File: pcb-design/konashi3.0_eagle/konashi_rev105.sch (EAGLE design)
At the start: 33 parts, among them CN1 ZX62-B-5PA(11), CN2 S2B-PH-K-S, CN3 WML-C69, CN4 MA05-2-2, CN7 BK-913, IC1 LP2981-30DBVR, IC2 ZLDO1117G50DITR-ND

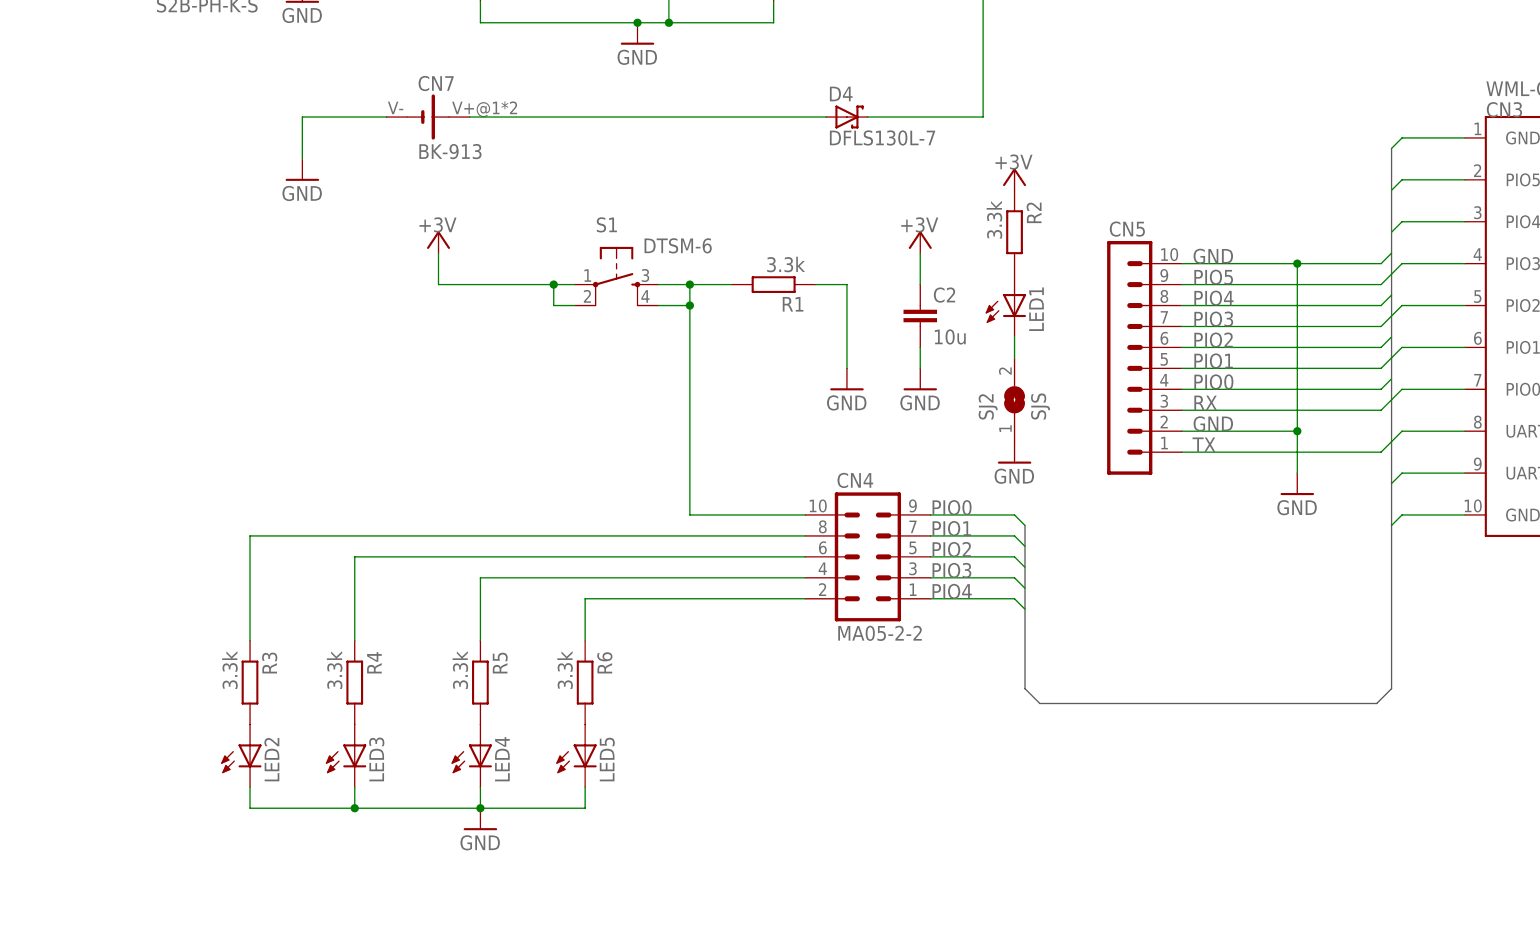
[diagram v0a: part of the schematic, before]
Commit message: 500kohm追加、ジャンパ用ピンヘッダ変更
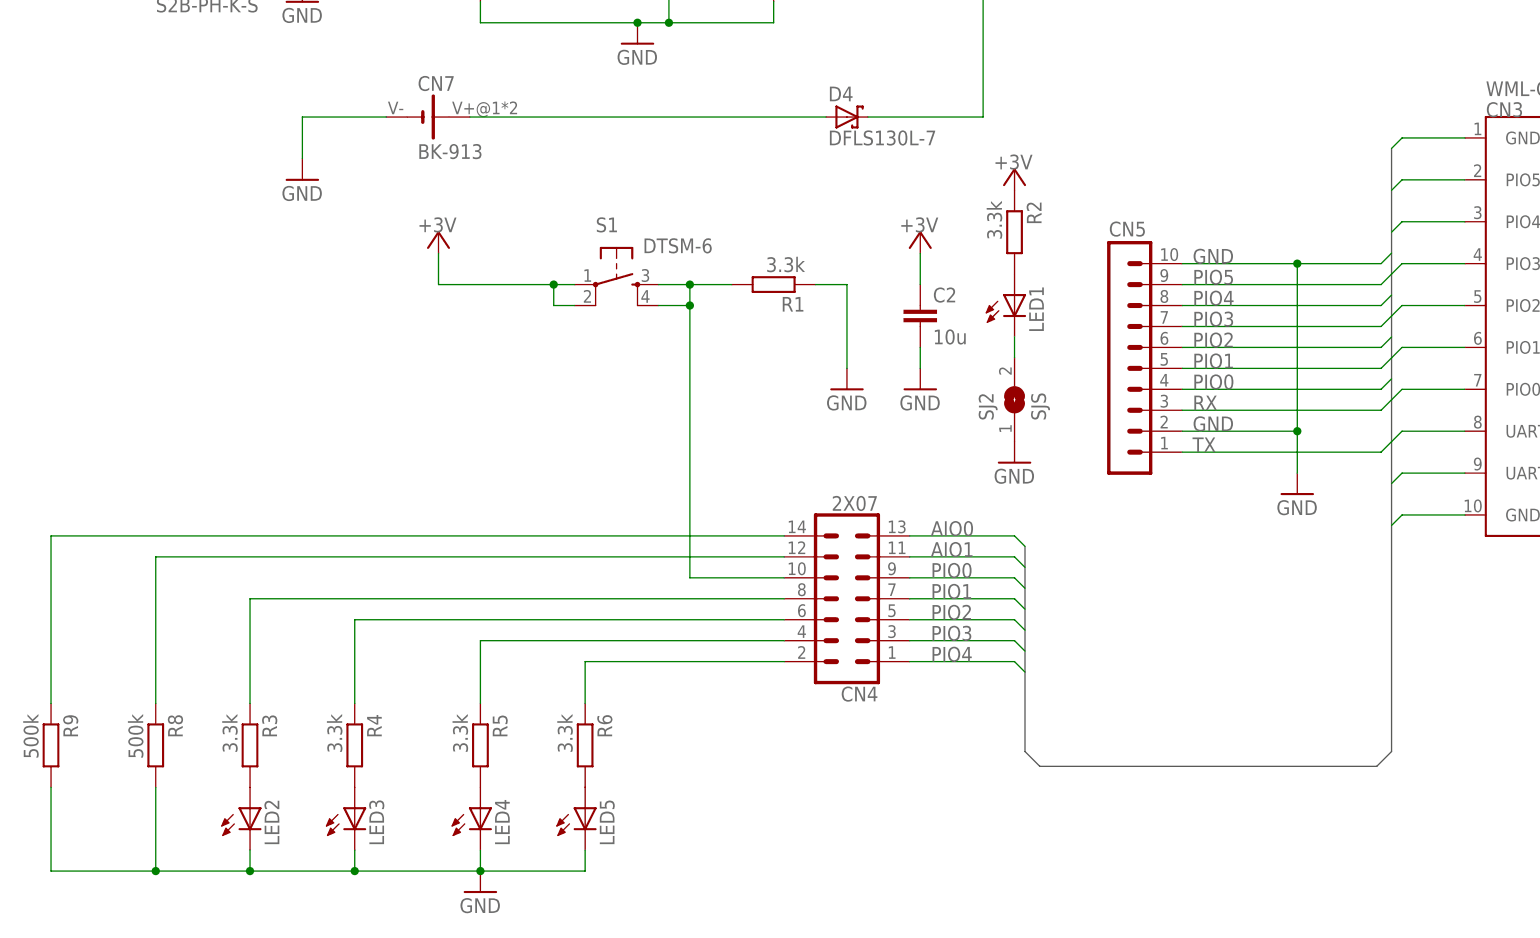
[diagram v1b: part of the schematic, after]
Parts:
- added R8, R9: 500k, rcl:R-EU_R0603
- CN4: value MA05-2-2 -> 2X07; device con-std:MA05-2-2 -> konashi_rev105:2X07
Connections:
- new net N$11: CN4.14, R9.1
- new net N$7: CN4.12, R8.1
- net AIO0: now also CN4.13
- net AIO1: now also CN4.11
- net GND: now also R8.2, R9.2
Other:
- moved on the sheet: LED2, LED3, LED4, LED5, R3, R4, R5, R6

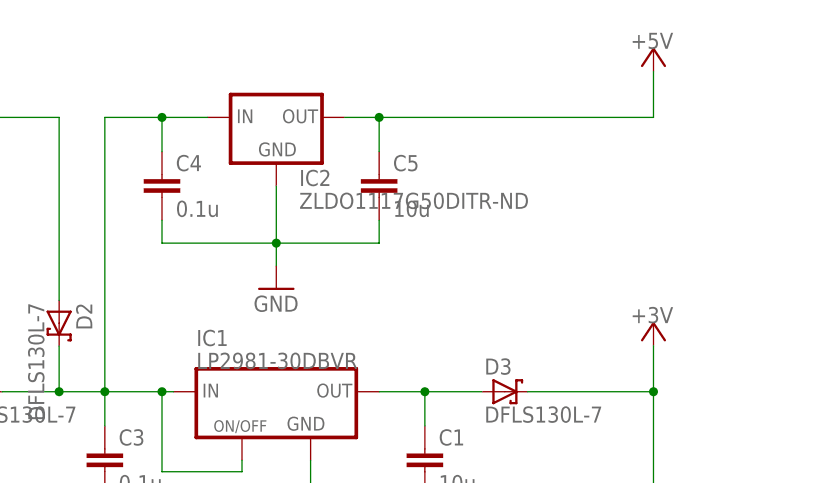
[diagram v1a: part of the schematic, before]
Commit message: ジャンパピンシルク追加等
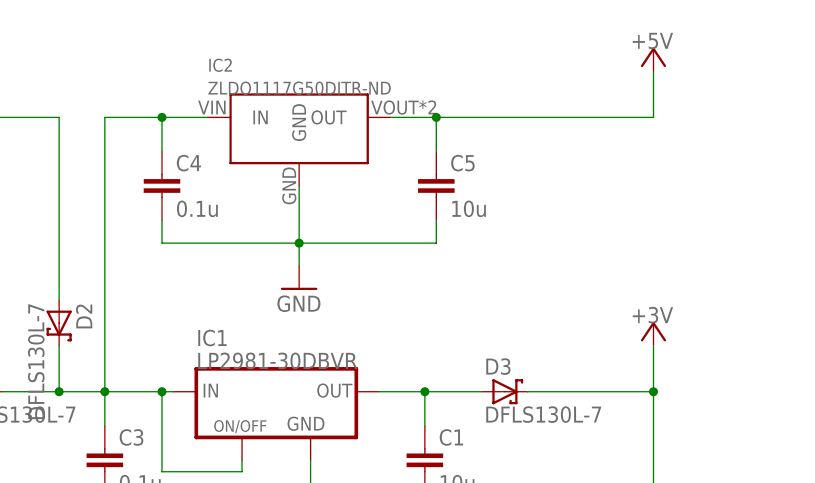
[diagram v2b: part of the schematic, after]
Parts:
- IC2: device LDO:ZLDO1117G50DITR-ND -> konashi_rev105:ZLDO1117G50DITR-ND
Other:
- moved on the sheet: C5
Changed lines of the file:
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@@
 <setting verticaltext="up"/>
 </settings>
-<grid distance="0.1" unitdist="inch" unit="inch" style="lines" multiple="1" display="no" altdistance="0.01" altunitdist="inch" altunit="inch"/>
+<grid distance="0.1" unitdist="inch" unit="inch" style="lines" multiple="1" display="yes" altdistance="0.01" altunitdist="inch" altunit="inch"/>
 <layers>
 <layer number="1" name="Top" color="4" fill="1" visible="no" active="no"/>
@@
 <part name="U$11" library="supply" deviceset="+5V" device=""/>
 <part name="GND7" library="supply" deviceset="GND" device=""/>
-<part name="IC2" library="LDO" deviceset="ZLDO1117G50DITR-ND" device=""/>
+<part name="IC2" library="konashi_rev105" deviceset="ZLDO1117G50DITR-ND" device=""/>
 <part name="CN2" library="con-jst" deviceset="S2B-PH-K-S" device=""/>
 <part name="R4" library="rcl" deviceset="R-EU_" device="R0603" value="3.3k"/>
@@
 <instance part="U$7" gate="G$1" x="254" y="129.54"/>
 <instance part="C4" gate="G$1" x="48.26" y="184.15"/>
-<instance part="C5" gate="G$1" x="72.39" y="184.15"/>
-<instance part="GND4" gate="G$1" x="60.96" y="171.45"/>
+<instance part="C5" gate="G$1" x="78.74" y="184.15"/>
+<instance part="GND4" gate="G$1" x="63.5" y="171.45"/>
 <instance part="U$9" gate="G$1" x="102.87" y="195.58"/>
 <instance part="GND6" gate="G$1" x="140.97" y="88.9"/>
 <instance part="U$11" gate="G$1" x="247.65" y="129.54"/>
 <instance part="GND7" gate="G$1" x="257.81" y="88.9"/>
-<instance part="IC2" gate="G$1" x="60.96" y="189.23"/>
+<instance part="IC2" gate="G$1" x="63.5" y="187.96" smashed="yes">
+<attribute name="NAME" x="53.34" y="195.58" size="1.4224" layer="95"/>
+<attribute name="VALUE" x="53.34" y="193.04" size="1.4224" layer="96"/>
+</instance>
 <instance part="CN2" gate="G$1" x="2.54" y="147.32"/>
 <instance part="R4" gate="G$1" x="26.67" y="58.42" rot="R270"/>
@@
 <segment>
 <pinref part="GND4" gate="G$1" pin="GND"/>
-<wire x1="60.96" y1="182.88" x2="60.96" y2="176.53" width="0.1524" layer="91"/>
+<wire x1="63.5" y1="182.88" x2="63.5" y2="176.53" width="0.1524" layer="91"/>
 <pinref part="C4" gate="G$1" pin="2"/>
-<wire x1="60.96" y1="176.53" x2="60.96" y2="173.99" width="0.1524" layer="91"/>
+<wire x1="63.5" y1="176.53" x2="63.5" y2="173.99" width="0.1524" layer="91"/>
 <wire x1="48.26" y1="179.07" x2="48.26" y2="176.53" width="0.1524" layer="91"/>
-<wire x1="48.26" y1="176.53" x2="60.96" y2="176.53" width="0.1524" layer="91"/>
+<wire x1="48.26" y1="176.53" x2="63.5" y2="176.53" width="0.1524" layer="91"/>
 <pinref part="C5" gate="G$1" pin="2"/>
-<wire x1="60.96" y1="176.53" x2="72.39" y2="176.53" width="0.1524" layer="91"/>
-<wire x1="72.39" y1="176.53" x2="72.39" y2="179.07" width="0.1524" layer="91"/>
-<junction x="60.96" y="176.53"/>
+<wire x1="63.5" y1="176.53" x2="78.74" y2="176.53" width="0.1524" layer="91"/>
+<wire x1="78.74" y1="176.53" x2="78.74" y2="179.07" width="0.1524" layer="91"/>
+<junction x="63.5" y="176.53"/>
 <pinref part="IC2" gate="G$1" pin="GND"/>
 </segment>
@@
 <segment>
 <pinref part="C5" gate="G$1" pin="1"/>
-<wire x1="72.39" y1="186.69" x2="72.39" y2="190.5" width="0.1524" layer="91"/>
-<wire x1="72.39" y1="190.5" x2="68.58" y2="190.5" width="0.1524" layer="91"/>
+<wire x1="78.74" y1="186.69" x2="78.74" y2="190.5" width="0.1524" layer="91"/>
+<wire x1="78.74" y1="190.5" x2="73.66" y2="190.5" width="0.1524" layer="91"/>
 <pinref part="U$9" gate="G$1" pin="+5V"/>
-<wire x1="72.39" y1="190.5" x2="102.87" y2="190.5" width="0.1524" layer="91"/>
+<wire x1="78.74" y1="190.5" x2="102.87" y2="190.5" width="0.1524" layer="91"/>
 <wire x1="102.87" y1="190.5" x2="102.87" y2="195.58" width="0.1524" layer="91"/>
-<junction x="72.39" y="190.5"/>
+<junction x="78.74" y="190.5"/>
 <pinref part="IC2" gate="G$1" pin="OUT"/>
 </segment>

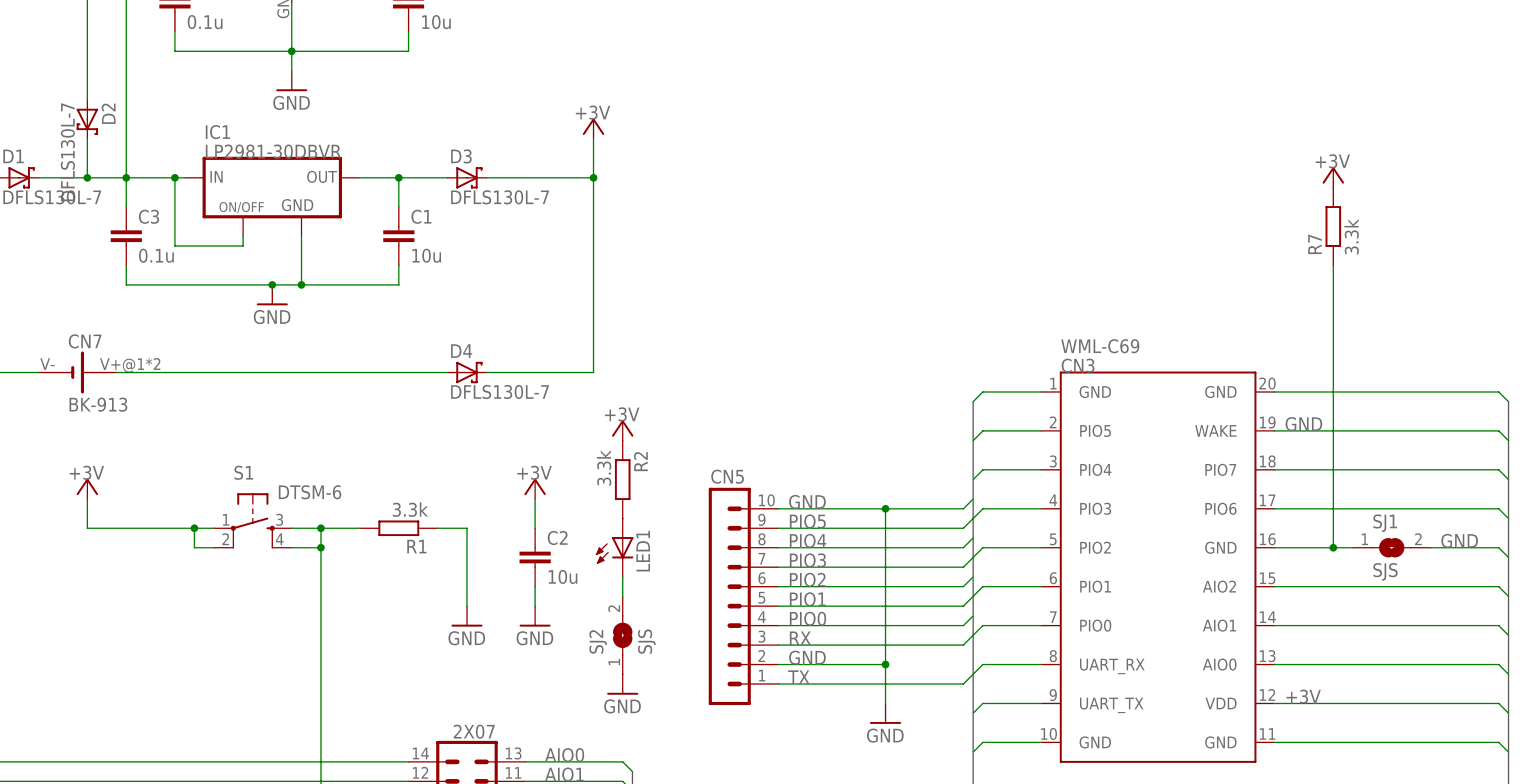
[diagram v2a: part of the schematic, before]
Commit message: ガーバーデータ追加、レギュレータ型番変更
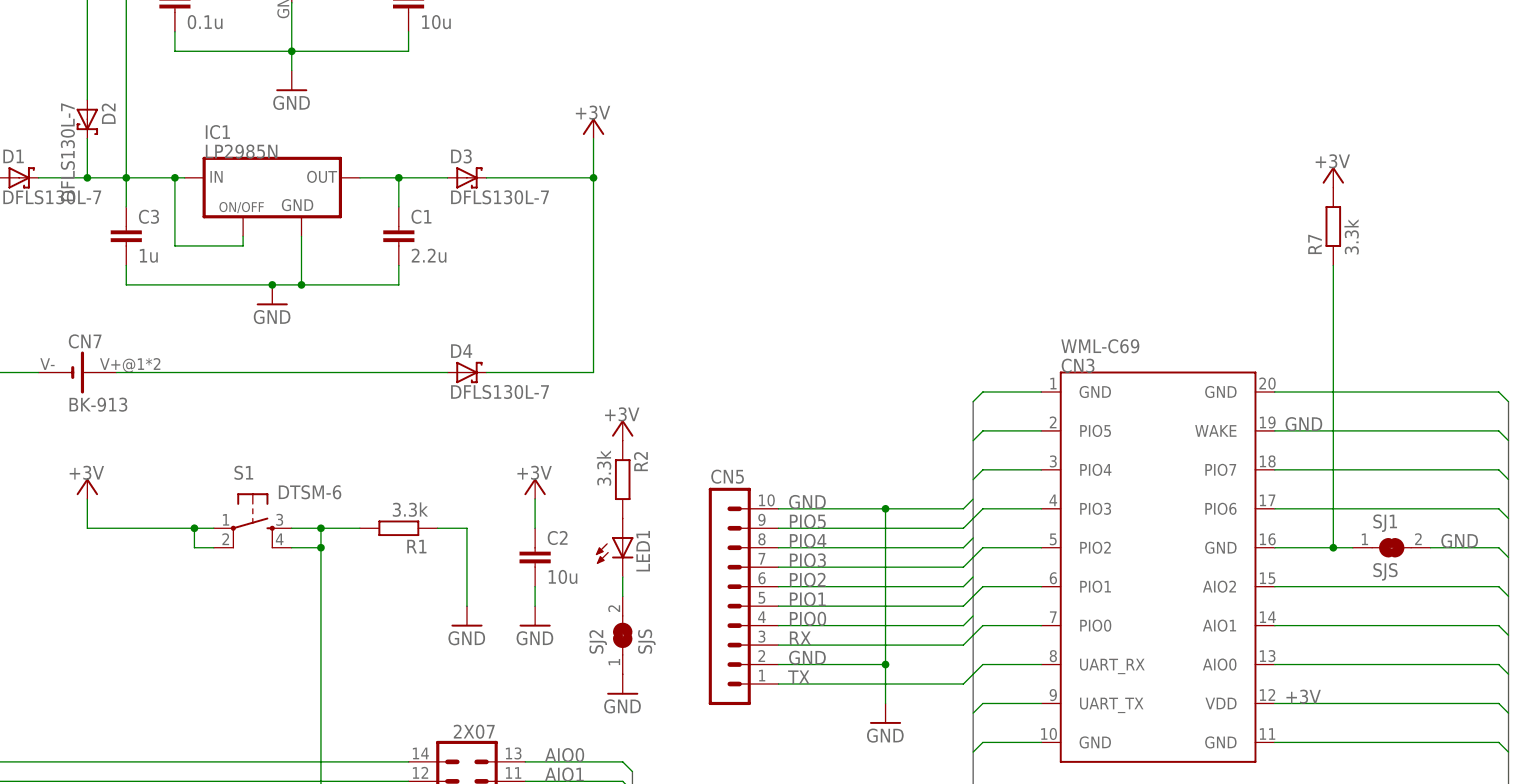
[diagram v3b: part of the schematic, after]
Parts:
- C1: value 10u -> 2.2u
- C3: value 0.1u -> 1u
- IC1: value LP2981-30DBVR -> LP2985N
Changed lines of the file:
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@@
 <setting verticaltext="up"/>
 </settings>
-<grid distance="0.1" unitdist="inch" unit="inch" style="lines" multiple="1" display="yes" altdistance="0.01" altunitdist="inch" altunit="inch"/>
+<grid distance="0.1" unitdist="inch" unit="inch" style="lines" multiple="1" display="no" altdistance="0.01" altunitdist="inch" altunit="inch"/>
 <layers>
 <layer number="1" name="Top" color="4" fill="1" visible="no" active="no"/>
@@
 <part name="R1" library="rcl" deviceset="R-EU_" device="R0603" value="3.3k"/>
 <part name="U$5" library="supply" deviceset="GND" device=""/>
-<part name="C1" library="rcl" deviceset="C-EU" device="C0603" value="10u"/>
-<part name="C3" library="rcl" deviceset="C-EU" device="C0603" value="0.1u"/>
+<part name="C1" library="rcl" deviceset="C-EU" device="C0603" value="2.2u"/>
+<part name="C3" library="rcl" deviceset="C-EU" device="C0603" value="1u"/>
 <part name="CN3" library="ble_CSR2" deviceset="WML-C69" device=""/>
 <part name="CN4" library="konashi_rev105" deviceset="2X07" device=""/>
@@
 <part name="R2" library="rcl" deviceset="R-EU_" device="R0603" value="3.3k"/>
 <part name="U$10" library="supply" deviceset="+3V" device=""/>
-<part name="IC1" library="LDO" deviceset="LP2981-30DBVR" device=""/>
+<part name="IC1" library="LDO" deviceset="LP2981-30DBVR" device="" value="LP2985N"/>
 <part name="CN7" library="con-CoinBatt" deviceset="BK-913" device=""/>
 <part name="SJ2" library="pad" deviceset="SJS" device=""/>
@@
 <sheet>
 <plain>
+<wire x1="106.68" y1="101.6" x2="106.68" y2="99.06" width="0.1524" layer="94"/>
+<wire x1="205.74" y1="111.76" x2="208.28" y2="111.76" width="0.1524" layer="94"/>
 </plain>
 <instances>

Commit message: BOM追加
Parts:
- IC1: value LP2985N -> LP2985IM5-3.6
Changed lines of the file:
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@@
 <part name="R2" library="rcl" deviceset="R-EU_" device="R0603" value="3.3k"/>
 <part name="U$10" library="supply" deviceset="+3V" device=""/>
-<part name="IC1" library="LDO" deviceset="LP2981-30DBVR" device="" value="LP2985N"/>
+<part name="IC1" library="LDO" deviceset="LP2981-30DBVR" device="" value="LP2985IM5-3.6"/>
 <part name="CN7" library="con-CoinBatt" deviceset="BK-913" device=""/>
 <part name="SJ2" library="pad" deviceset="SJS" device=""/>
